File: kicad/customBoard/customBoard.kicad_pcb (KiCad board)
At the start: 2 copper layers, 77 parts, among them J1 USB4125-GF-A_REVA2, J2 SS-53000-001, J3 FFC3B07-20-T, J4 Micro_SD_Card_Det, J5 ARJM11D7-502-AB-EW2, J6 SS-52100-001, J7 SS-52100-001, J8 SS-52100-001, J9 FFC3B07-20-T, Q1 MMUN2133LT1G, U1 TPS61090RSAR, U2 MCP73871-2CCI_ML, U3 74LVC1G07, U4 RT9742VGJ5, U5 RT9742ENGJ5, U6 TPD4EUSB30, U7 TPD4EUSB30, U8 USB2504A-JT, U9 AP22653W6-7, Y1 24MHz

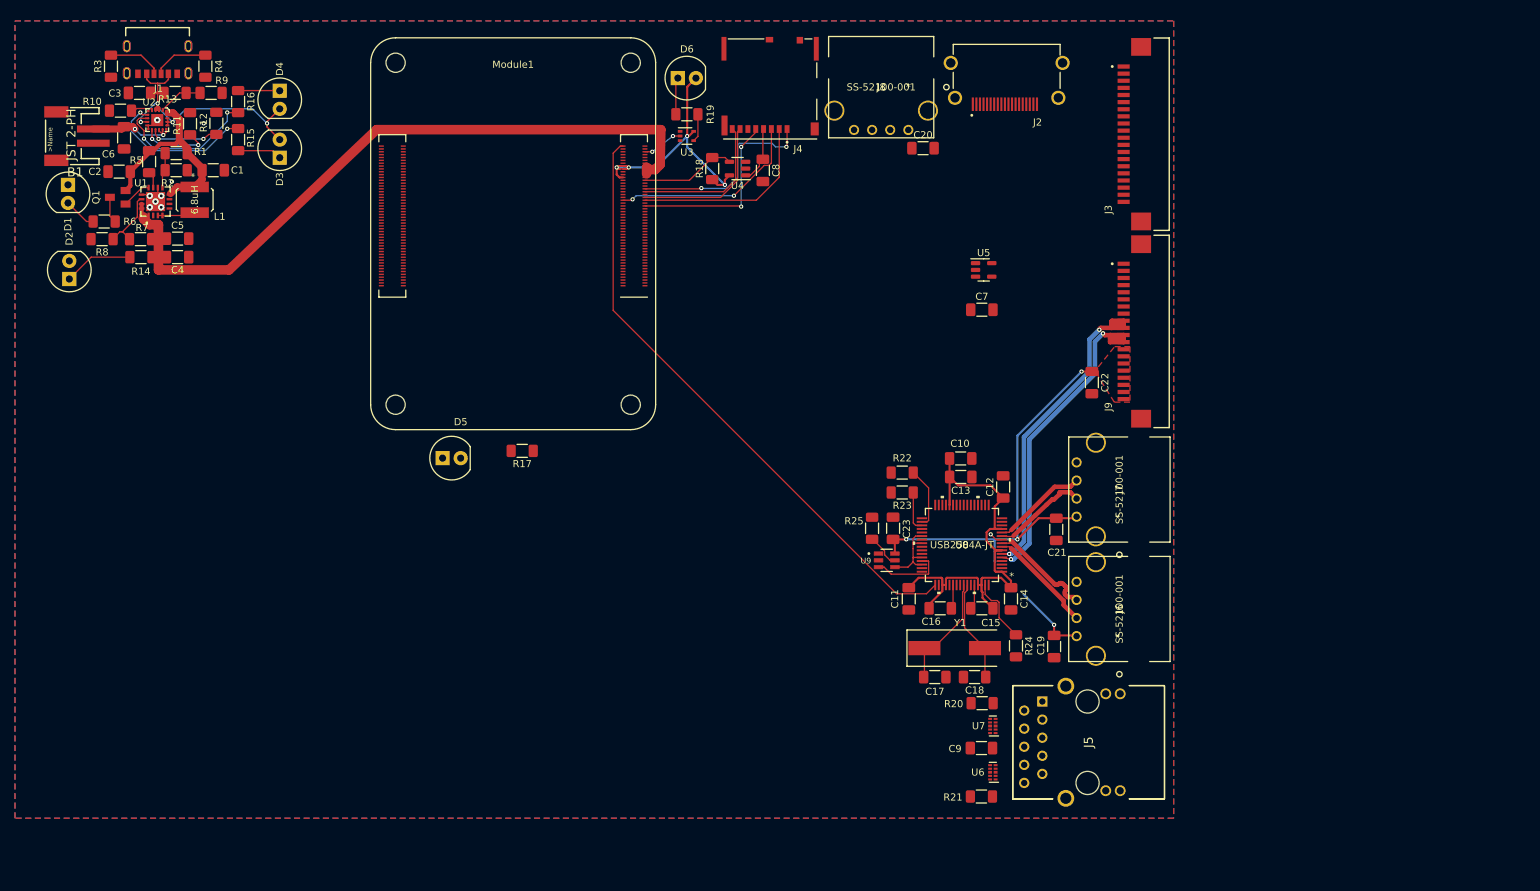
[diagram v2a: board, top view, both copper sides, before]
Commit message: Draft HDMI and more differential pairs
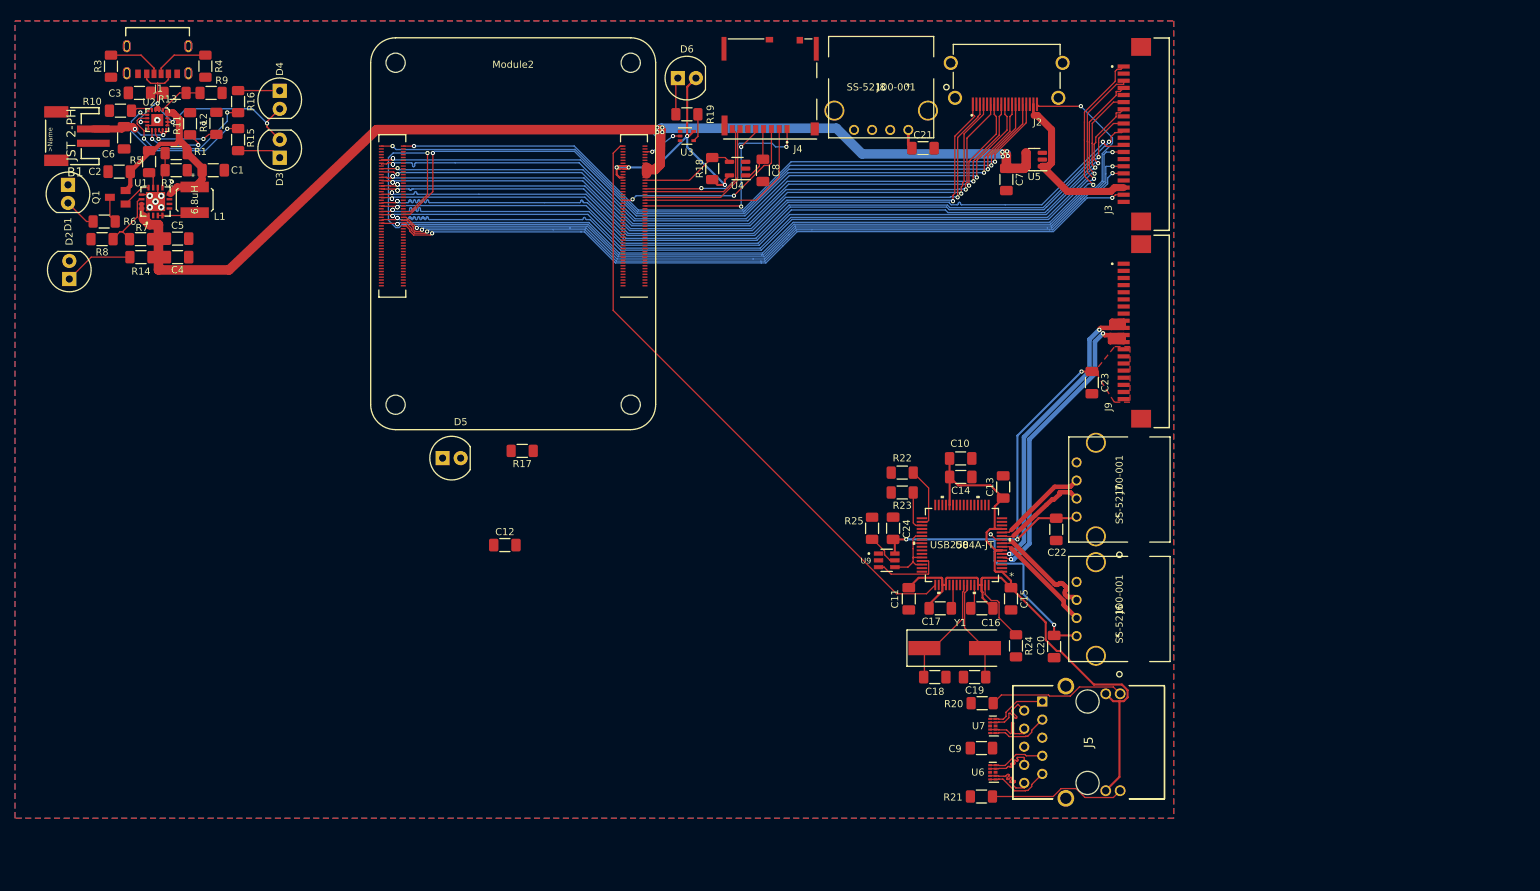
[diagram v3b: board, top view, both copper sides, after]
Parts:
- added C12: 100n, Capacitor_SMD:C_1206_3216Metric_Pad1.33x1.80mm_HandSolder, F.Cu at (92.3, 91.7)
- moved C7 18.6 mm to (162.7, 40.4), turned to -90 degrees
- moved U5 17.0 mm to (166.6, 37.6), turned to 180 degrees
- renumbered C12 to C13, C13 to C14, C14 to C15, C15 to C16, C16 to C17, C17 to C18, C18 to C19, C19 to C20, C20 to C21, C21 to C22, C22 to C23, C23 to C24, Module1 to Module2
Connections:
- C19 pad 1: Net-(C18-Pad1) (its old number) -> (no net)
- Module2 pad 103: unconnected-(Module1-Pad103) -> /CM4/USB2_N
- Module2 pad 105: unconnected-(Module1-Pad105) -> /CM4/USB2_P
- Module2 pad 107: unconnected-(Module1-Pad107) -> GND
- Module2 pad 108: unconnected-(Module1-Pad108) -> GND
- Module2 pad 113: unconnected-(Module1-Pad113) -> GND
- Module2 pad 114: unconnected-(Module1-Pad114) -> GND
- Module2 pad 119: unconnected-(Module1-Pad119) -> GND
- Module2 pad 120: unconnected-(Module1-Pad120) -> GND
- Module2 pad 125: unconnected-(Module1-Pad125) -> GND
- Module2 pad 126: unconnected-(Module1-Pad126) -> GND
- Module2 pad 131: unconnected-(Module1-Pad131) -> GND
- Module2 pad 132: unconnected-(Module1-Pad132) -> GND
- Module2 pad 137: unconnected-(Module1-Pad137) -> GND
- Module2 pad 138: unconnected-(Module1-Pad138) -> GND
- Module2 pad 143: unconnected-(Module1-Pad143) -> /CM4/HDMI1_HOTPLUG
- Module2 pad 144: unconnected-(Module1-Pad144) -> GND
- Module2 pad 145: unconnected-(Module1-Pad145) -> /CM4/HDMI1_SDA
- Module2 pad 146: unconnected-(Module1-Pad146) -> /CM4/HDMI1_D2_P
- Module2 pad 147: unconnected-(Module1-Pad147) -> /CM4/HDMI1_SCL
- Module2 pad 148: unconnected-(Module1-Pad148) -> /CM4/HDMI1_D2_N
- Module2 pad 149: unconnected-(Module1-Pad149) -> /CM4/HDMI1_CEC
- Module2 pad 150: unconnected-(Module1-Pad150) -> GND
- Module2 pad 151: unconnected-(Module1-Pad151) -> /CM4/HDMI0_CEC
- Module2 pad 152: unconnected-(Module1-Pad152) -> /CM4/HDMI1_D1_P
- Module2 pad 153: unconnected-(Module1-Pad153) -> /CM4/HDMI0_HOTPLUG
- Module2 pad 154: unconnected-(Module1-Pad154) -> /CM4/HDMI1_D1_N
- Module2 pad 155: unconnected-(Module1-Pad155) -> GND
- Module2 pad 156: unconnected-(Module1-Pad156) -> GND
- Module2 pad 158: unconnected-(Module1-Pad158) -> /CM4/HDMI1_D0_P
- Module2 pad 160: unconnected-(Module1-Pad160) -> /CM4/HDMI1_D0_N
- Module2 pad 161: unconnected-(Module1-Pad161) -> GND
- Module2 pad 162: unconnected-(Module1-Pad162) -> GND
- Module2 pad 164: unconnected-(Module1-Pad164) -> /CM4/HDMI1_CK_P
- Module2 pad 166: unconnected-(Module1-Pad166) -> /CM4/HDMI1_CK_N
- Module2 pad 167: unconnected-(Module1-Pad167) -> GND
- Module2 pad 168: unconnected-(Module1-Pad168) -> GND
- Module2 pad 170: unconnected-(Module1-Pad170) -> /CM4/HDMI0_D2_P
- Module2 pad 172: unconnected-(Module1-Pad172) -> /CM4/HDMI0_D2_N
- Module2 pad 173: unconnected-(Module1-Pad173) -> GND
- Module2 pad 174: unconnected-(Module1-Pad174) -> GND
- Module2 pad 176: unconnected-(Module1-Pad176) -> /CM4/HDMI0_D1_P
- Module2 pad 178: unconnected-(Module1-Pad178) -> /CM4/HDMI0_D1_N
- Module2 pad 179: unconnected-(Module1-Pad179) -> GND
- Module2 pad 180: unconnected-(Module1-Pad180) -> GND
- Module2 pad 182: unconnected-(Module1-Pad182) -> /CM4/HDMI0_D0_P
- Module2 pad 184: unconnected-(Module1-Pad184) -> /CM4/HDMI0_D0_N
- Module2 pad 185: unconnected-(Module1-Pad185) -> GND
- Module2 pad 186: unconnected-(Module1-Pad186) -> GND
- Module2 pad 188: unconnected-(Module1-Pad188) -> /CM4/HDMI0_CK_P
- Module2 pad 190: unconnected-(Module1-Pad190) -> /CM4/HDMI0_CK_N
- Module2 pad 191: unconnected-(Module1-Pad191) -> GND
- Module2 pad 192: unconnected-(Module1-Pad192) -> GND
- Module2 pad 197: unconnected-(Module1-Pad197) -> GND
- Module2 pad 198: unconnected-(Module1-Pad198) -> GND
- Module2 pad 199: unconnected-(Module1-Pad199) -> /CM4/HDMI0_SDA
- Module2 pad 200: unconnected-(Module1-Pad200) -> /CM4/HDMI0_SCL
- U8 pad 58: Net-(C18-Pad1) (its old number) -> Net-(C19-Pad1)
- Y1 pad 2: Net-(C18-Pad1) (its old number) -> Net-(C19-Pad1)
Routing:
- net /CM4/HDMI0_HOTPLUG: track 0.00 -> 150.8 mm, vias 0 -> 2
- net /CM4/HDMI1_D2_P: track 0.00 -> 126.0 mm, vias 0 -> 3
- net /CM4/HDMI1_D2_N: track 0.00 -> 125.8 mm, vias 0 -> 3
- net /CM4/HDMI1_D1_P: track 0.00 -> 121.3 mm, vias 0 -> 3
- net /CM4/HDMI1_D1_N: track 0.00 -> 121.3 mm, vias 0 -> 3
- net /CM4/HDMI1_D0_P: track 0.00 -> 118.2 mm, vias 0 -> 3
- net /CM4/HDMI1_D0_N: track 0.00 -> 118.1 mm, vias 0 -> 3
- net /CM4/HDMI1_CK_P: track 0.00 -> 114.2 mm, vias 0 -> 3
- net /CM4/HDMI1_CK_N: track 0.00 -> 114.1 mm, vias 0 -> 3
- net /CM4/HDMI1_CEC: track 0.00 -> 112.0 mm, vias 0 -> 2
- net /CM4/HDMI1_SCL: track 0.00 -> 110.8 mm, vias 0 -> 2
- net /CM4/HDMI1_SDA: track 0.00 -> 109.5 mm, vias 0 -> 2
- net /CM4/HDMI1_HOTPLUG: track 0.00 -> 107.7 mm, vias 0 -> 2
- net /CM4/HDMI0_CEC: track 0.00 -> 105.9 mm, vias 0 -> 2
- net /CM4/HDMI0_CK_P: track 0.00 -> 102.7 mm, vias 0 -> 3
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
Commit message: Draft before fixing errors
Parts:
- removed C12: 100n, Capacitor_SMD:C_1206_3216Metric_Pad1.33x1.80mm_HandSolder
- moved D5 58.4 mm to (109.8, 26.2), turned to 180 degrees
- moved R17 50.3 mm to (110.8, 30.9), turned to 0 degrees
- moved Module2 7.03 mm to (102.9, 24.0)
- moved R25 1.54 mm to (144.8, 88.1)
- moved C24 0.49 mm to (147.2, 89.2)
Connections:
- U6 pad 10: unconnected-(U6-Pad10) -> /CM4/TRD3_P
- U6 pad 6: unconnected-(U6-Pad6) -> /CM4/TRD2_P
- U6 pad 7: unconnected-(U6-Pad7) -> /CM4/TRD2_N
- U6 pad 9: unconnected-(U6-Pad9) -> /CM4/TRD3_N
- U7 pad 10: unconnected-(U7-Pad10) -> /CM4/TRD1_P
- U7 pad 6: unconnected-(U7-Pad6) -> /CM4/TRD0_P
- U7 pad 7: unconnected-(U7-Pad7) -> /CM4/TRD0_N
- U7 pad 9: unconnected-(U7-Pad9) -> /CM4/TRD1_N
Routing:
- net /CM4/TRD2_P: track 8.07 -> 125.6 mm, vias 0 -> 4
- net /CM4/TRD2_N: track 8.00 -> 122.6 mm, vias 0 -> 6
- net +3V3: track 143.9 -> 258.3 mm, vias 4 -> 8
- net /CM4/USB2_N: track 0.00 -> 112.8 mm, vias 0 -> 3
- net /CM4/USB2_P: track 0.00 -> 112.2 mm, vias 0 -> 3
- net /CM4/ETH_LEDG: track 0.00 -> 109.0 mm, vias 0 -> 2
- net /CM4/TRD3_N: track 9.11 -> 116.1 mm, vias 0 -> 3
- net /CM4/TRD3_P: track 9.19 -> 115.6 mm, vias 0 -> 3
- net /CM4/ETH_LEDY: track 0.00 -> 96.0 mm, vias 0 -> 2
- net /CM4/TRD0_N: track 8.70 -> 100.3 mm, vias 0 -> 2
- net /CM4/TRD1_P: track 8.73 -> 99.4 mm
- net /CM4/TRD1_N: track 8.70 -> 99.2 mm
- net /CM4/TRD0_P: track 8.73 -> 99.0 mm
- net /USB/D4_N: track 0.00 -> 65.2 mm
- net /USB/D4_P: track 0.00 -> 65.2 mm
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
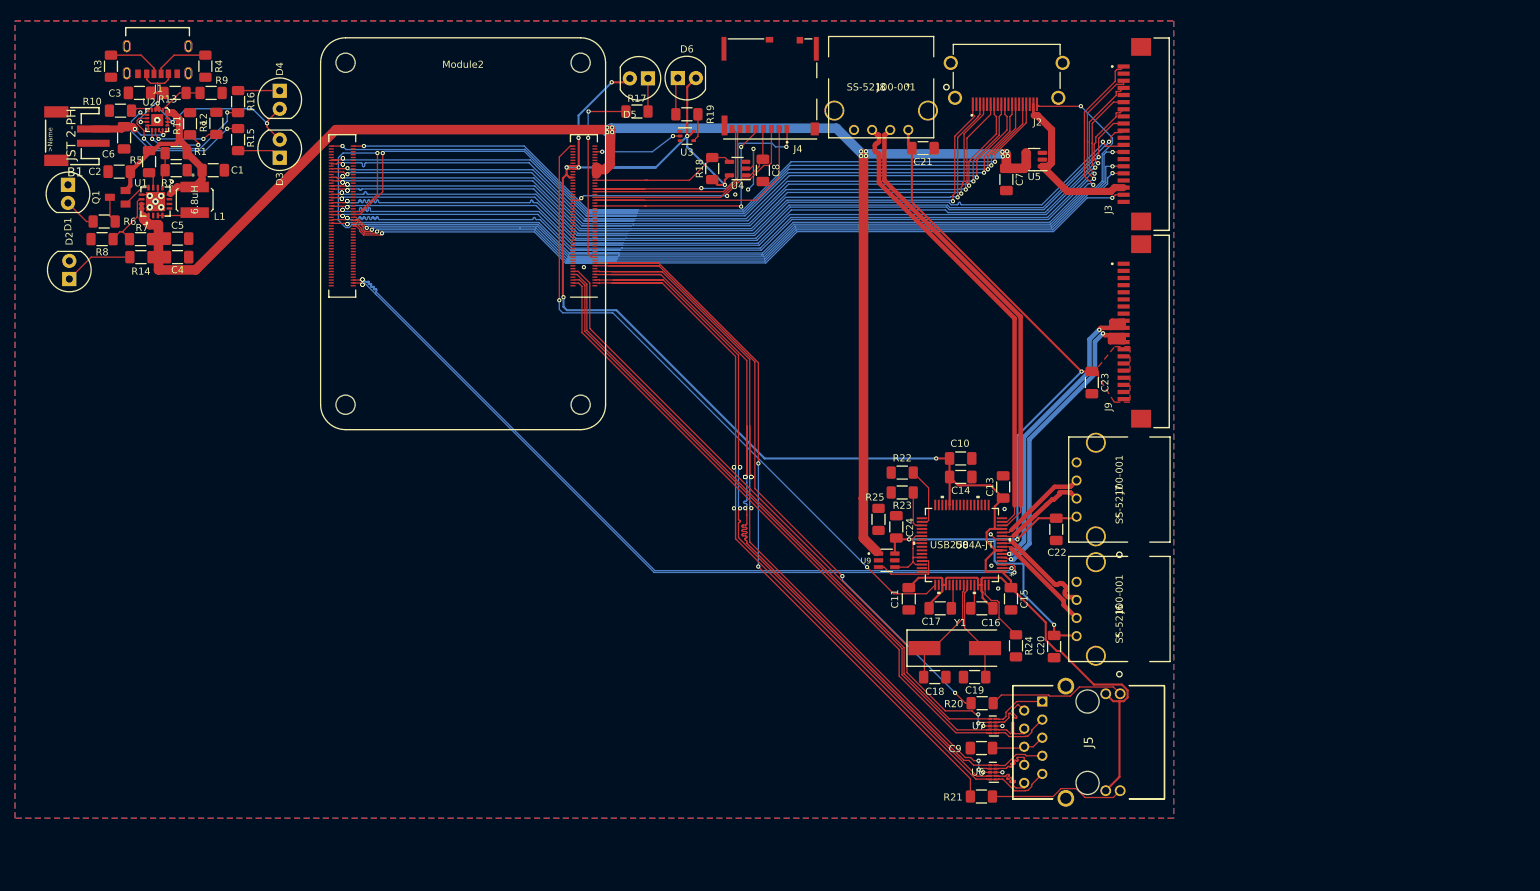
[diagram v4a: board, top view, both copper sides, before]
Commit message: Fix errors with draft
Now I need to run it by a bunch of people, but from my point of view, I don't know what else to do before the fabrication step
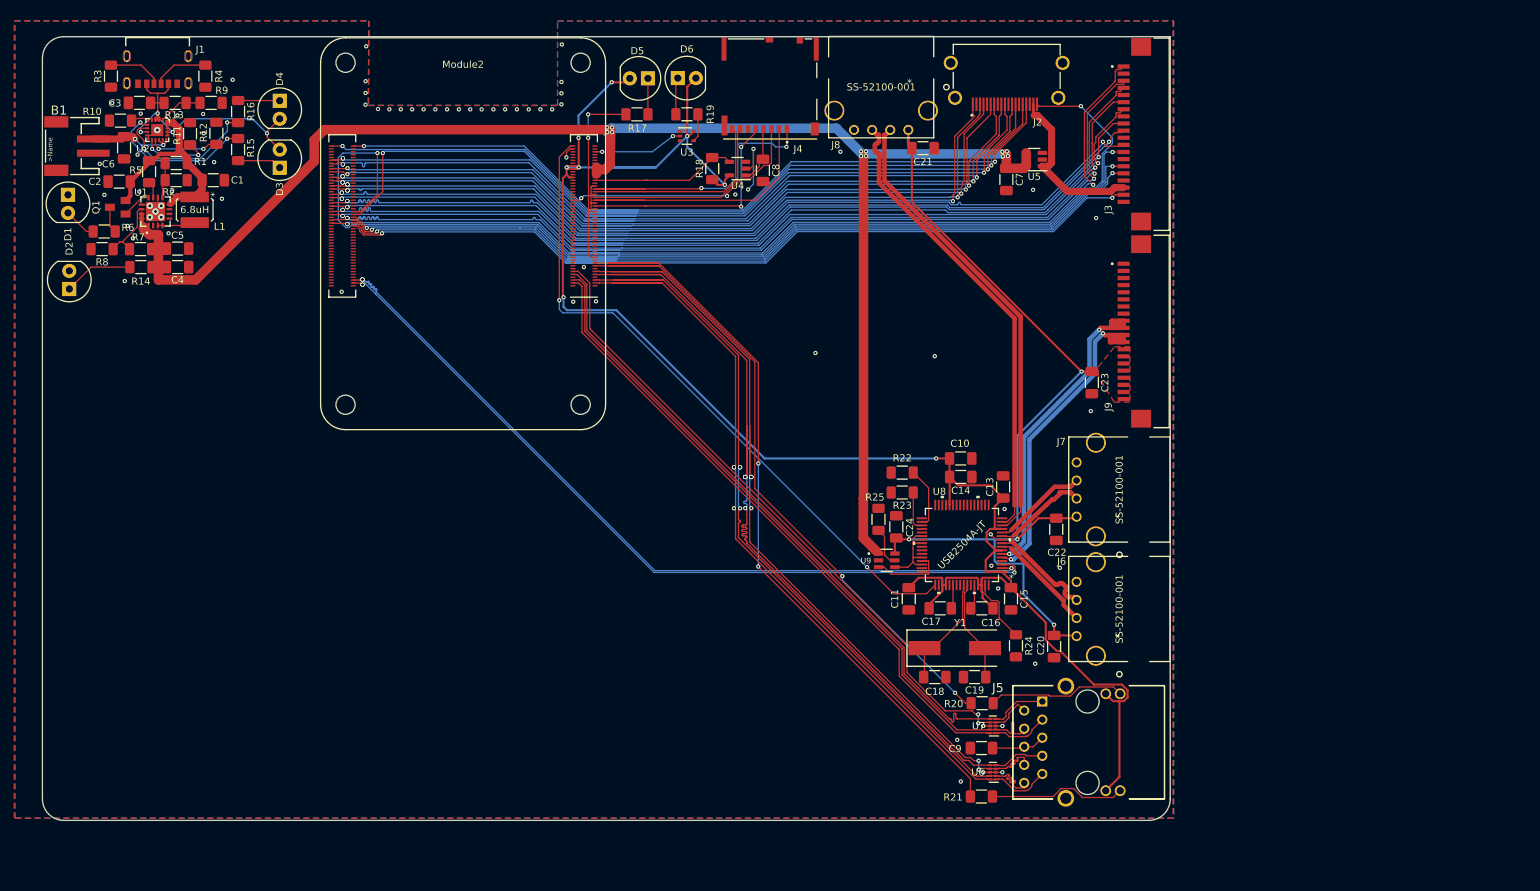
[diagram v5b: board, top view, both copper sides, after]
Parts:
- moved B1 1.40 mm to (30.8, 35.7)
- moved C6 1.40 mm to (38.9, 35.9)
- moved L1 1.40 mm to (48.8, 44.6)
- moved R11 1.40 mm to (48.1, 34.0)
- moved U1 1.40 mm to (43.3, 44.9)
- moved U2 1.40 mm to (43.5, 33.5)
- moved J1 1.40 mm to (43.6, 23.9)
- moved R16 1.40 mm to (54.9, 30.9)
- moved C1 1.40 mm to (51.4, 40.5)
- moved C2 1.40 mm to (38.2, 40.7)
- moved C3 1.40 mm to (41.0, 29.6)
- moved C4 1.40 mm to (46.4, 52.7)
- moved C5 1.40 mm to (46.4, 50.1)
- moved D1 1.40 mm to (31.0, 45.1)
- moved D2 1.40 mm to (31.2, 53.2)
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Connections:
- C19 pad 1: (no net) -> Net-(C19-Pad1)
- U6 pad 10: /CM4/TRD3_P -> unconnected-(U6-Pad10)
- U6 pad 6: /CM4/TRD2_P -> unconnected-(U6-Pad6)
- U6 pad 7: /CM4/TRD2_N -> unconnected-(U6-Pad7)
- U6 pad 9: /CM4/TRD3_N -> unconnected-(U6-Pad9)
- U7 pad 10: /CM4/TRD1_P -> unconnected-(U7-Pad10)
- U7 pad 6: /CM4/TRD0_P -> unconnected-(U7-Pad6)
- U7 pad 7: /CM4/TRD0_N -> unconnected-(U7-Pad7)
- U7 pad 9: /CM4/TRD1_N -> unconnected-(U7-Pad9)
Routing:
- net GND: track 23.4 -> 31.3 mm, vias 20 -> 73
- net Net-(R25-Pad1): track 0.66 -> 5.54 mm
- net /CM4/5v: track 212.9 -> 215.2 mm
- net /CM4/TRD0_N: track 100.3 -> 98.1 mm
- net /CM4/TRD0_P: track 99.0 -> 101.1 mm
- net /USB/D1_P: track 46.9 -> 48.6 mm
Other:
- board outline added: 158.3 x 110 mm
